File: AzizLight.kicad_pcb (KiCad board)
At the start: 2 copper layers, 70.1 x 29.2 mm, 58 parts, among them P1 +9V, Q1 BS170, Q2 BS170, Q3 BS170, Q4 BS170, SW1 Reset, SW2 Invert, U1 MCP602, U2 LM393, U3 MCP601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

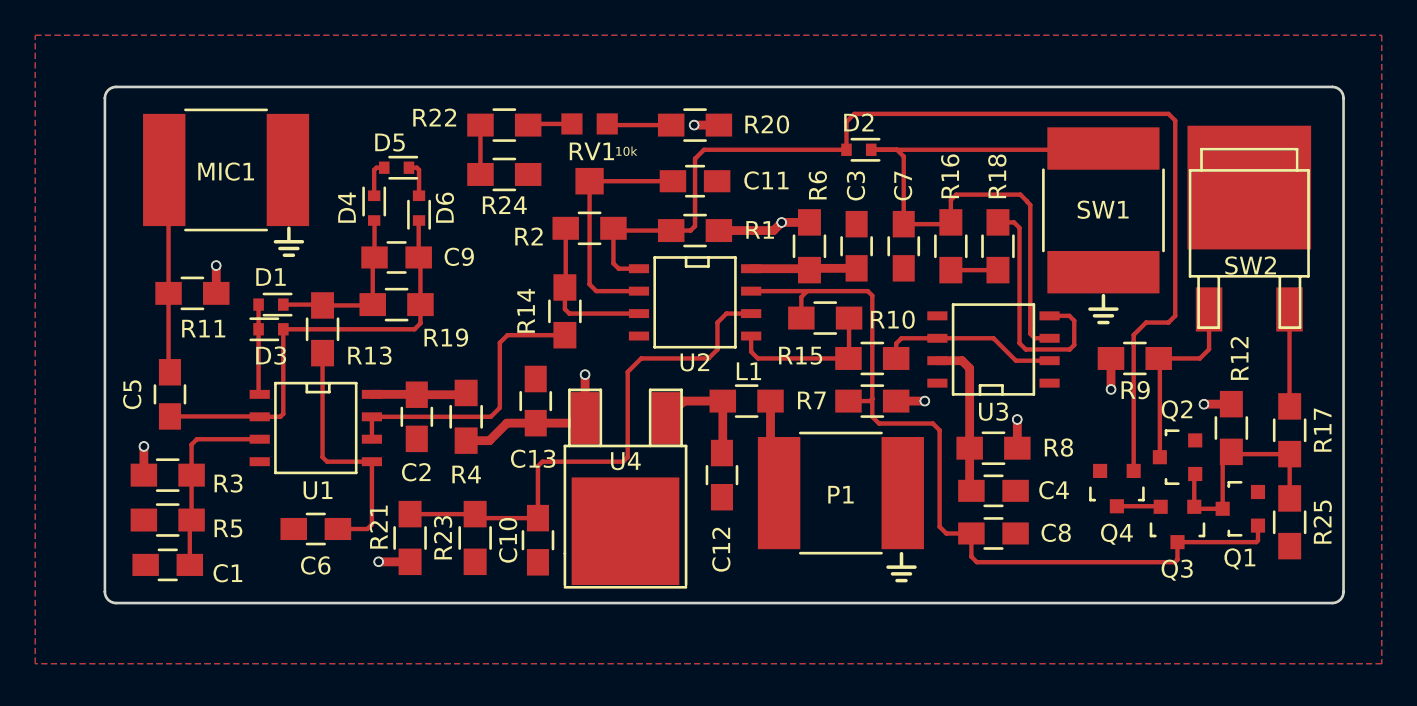
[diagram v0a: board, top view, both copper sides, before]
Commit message: Updated PCB for more efficient layout
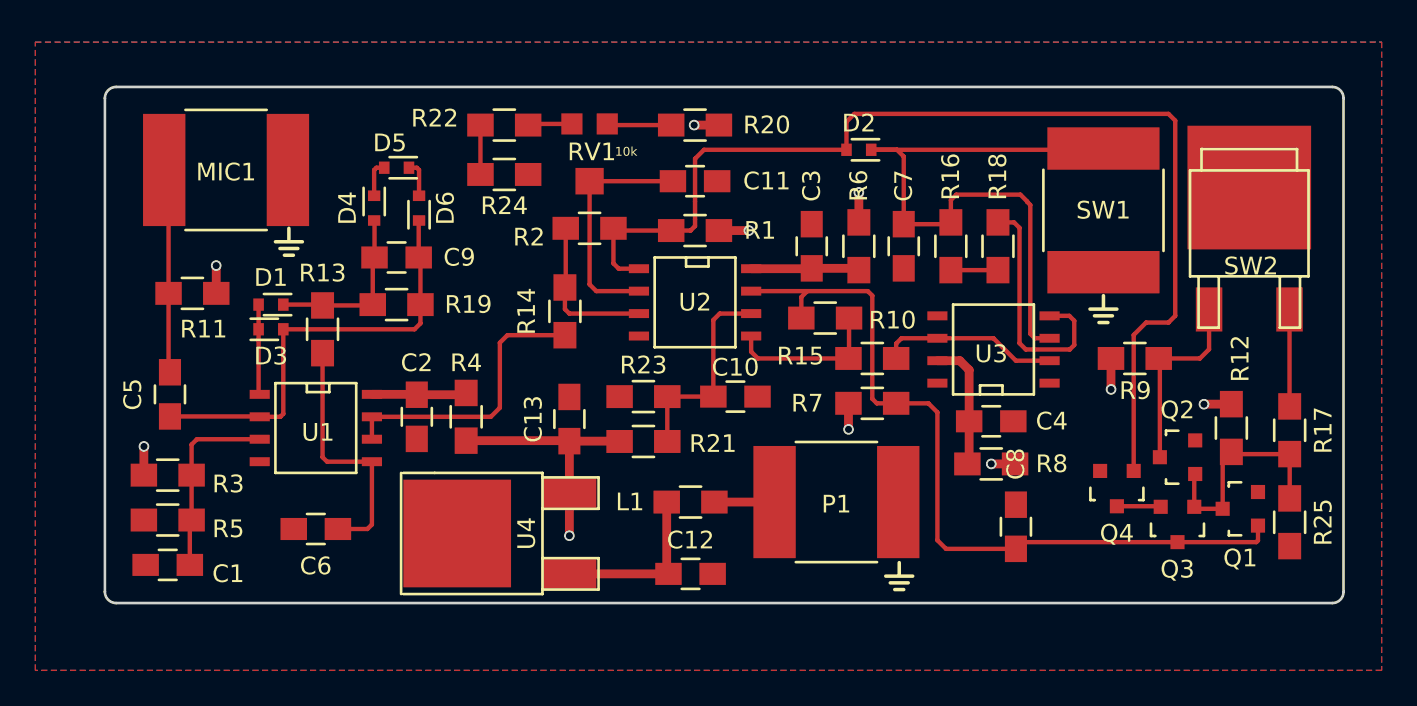
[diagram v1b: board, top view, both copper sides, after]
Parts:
- moved R21 14.3 mm to (146.2, 96.6), turned to 0 degrees
- moved C10 13.8 mm to (151.4, 94.1), turned to 0 degrees
- moved R23 12.4 mm to (146.2, 94.1), turned to 0 degrees
- moved U4 7.21 mm to (142.0, 101.9), turned to 90 degrees
- moved L1 6.54 mm to (148.8, 100.1)
- moved C12 5.86 mm to (148.8, 104.1), turned to 0 degrees
- moved C4 3.94 mm to (165.9, 95.5)
- moved R6 2.79 mm to (158.4, 85.6)
- moved C3 2.54 mm to (155.7, 85.6)
- moved C13 2.16 mm to (142.0, 95.4)
- moved C8 1.33 mm to (167.3, 101.5), turned to 90 degrees
- moved R8 0.90 mm to (165.9, 97.9)
- moved P1 0.57 mm to (157.1, 100.1)
- moved R7 0.13 mm to (159.1, 94.5), turned to 0 degrees
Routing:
- net Net-(C10-Pad1): track 29.6 -> 11.8 mm
- net Net-(C12-Pad1): track 6.78 -> 9.71 mm
- net Net-(C8-Pad1): track 48.0 -> 45.1 mm
- net Net-(L1-Pad1): track 5.41 -> 3.41 mm
- net Net-(C4-Pad2): track 8.98 -> 7.37 mm

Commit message: Updated README
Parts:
- moved C13 0.25 mm to (141.7, 95.4)
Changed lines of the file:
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@@
     (thickness 1.6)
     (drawings 20)
-    (tracks 215)
+    (tracks 218)
     (zones 0)
     (modules 58)
@@
   )
   (module Capacitors_SMD:C_0805_HandSoldering (layer F.Cu)
-    (at 141.986 95.377 90)
+    (at 141.732 95.377 90)
     (descr "Capacitor SMD 0805, hand soldering")
     (tags "capacitor 0805")
@@
   (segment (start 147.494 100.076) (end 147.494 104.04) (width 0.5) (layer F.Cu) (net 14))
   (segment (start 147.494 104.04) (end 147.594 104.14) (width 0.5) (layer F.Cu) (net 14))
+  (segment (start 150.448 78.74) (end 149.098 78.74) (width 0.5) (layer F.Cu) (net 15))
+  (via (at 149.098 78.74) (size 0.6) (drill 0.4) (layers F.Cu B.Cu) (net 15))
+  (segment (start 144.827 96.647) (end 141.752 96.647) (width 0.5) (layer F.Cu) (net 15))
+  (segment (start 141.752 96.647) (end 141.732 96.627) (width 0.5) (layer F.Cu) (net 15))
+  (segment (start 136.144 96.6) (end 141.705 96.6) (width 0.5) (layer F.Cu) (net 15))
+  (segment (start 141.705 96.6) (end 141.732 96.627) (width 0.5) (layer F.Cu) (net 15))
+  (segment (start 141.986 99.568) (end 141.986 96.881) (width 0.5) (layer F.Cu) (net 15))
+  (segment (start 141.986 96.881) (end 141.732 96.627) (width 0.5) (layer F.Cu) (net 15))
   (segment (start 157.781 94.488) (end 157.781 95.9574) (width 0.5) (layer F.Cu) (net 15))
   (via (at 157.7848 95.9612) (size 0.6) (drill 0.4) (layers F.Cu B.Cu) (net 15))
@@
   (segment (start 158.369 84.248) (end 158.369 82.55) (width 0.5) (layer F.Cu) (net 15))
   (via (at 158.369 82.55) (size 0.6) (drill 0.4) (layers F.Cu B.Cu) (net 15))
-  (segment (start 141.986 96.627) (end 144.807 96.627) (width 0.5) (layer F.Cu) (net 15))
   (segment (start 144.807 96.627) (end 144.827 96.647) (width 0.5) (layer F.Cu) (net 15))
-  (segment (start 141.986 96.627) (end 141.986 99.568) (width 0.5) (layer F.Cu) (net 15))
-  (segment (start 136.144 96.6) (end 141.959 96.6) (width 0.5) (layer F.Cu) (net 15))
   (segment (start 141.959 96.6) (end 141.986 96.627) (width 0.5) (layer F.Cu) (net 15))
   (segment (start 141.986 99.568) (end 141.986 101.981) (width 0.5) (layer F.Cu) (net 15))
@@
   (via (at 172.6438 93.7006) (size 0.6) (drill 0.4) (layers F.Cu B.Cu) (net 15))
   (segment (start 172.64 93.6968) (end 172.6438 93.7006) (width 0.5) (layer F.Cu) (net 15))
-  (segment (start 150.448 78.74) (end 149.0472 78.74) (width 0.5) (layer F.Cu) (net 15))
-  (via (at 149.0472 78.74) (size 0.6) (drill 0.4) (layers F.Cu B.Cu) (net 15))
   (segment (start 117.903 98.552) (end 117.903 96.9302) (width 0.5) (layer F.Cu) (net 15))
   (via (at 117.9068 96.9264) (size 0.6) (drill 0.4) (layers F.Cu B.Cu) (net 15))

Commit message: Modified SW2 solder pads.
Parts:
- R17: value 4.7k -> 100
- SW2: value Invert -> Trigger Out; footprint TO_SOT_Packages_SMD:SOT-428 -> Capacitors_SMD:C_2225_HandSoldering
- moved SW2 2.33 mm to (181.3, 83.6), turned to 270 degrees
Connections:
- SW2 pad 2: Switch -> Net-(R17-Pad1)
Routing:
- net Net-(Q2-Pad3): track 11.0 -> 23.0 mm
- net Net-(R17-Pad1): track 5.49 -> 8.32 mm
